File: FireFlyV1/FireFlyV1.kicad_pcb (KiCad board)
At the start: 2 copper layers, 64 x 26.2 mm, 59 parts, among them J1 Conn_01x03, J2 Conn_01x01_Pin, J3 Conn_01x01_Pin, SW1 TS-1187A-B-A-B, SW2 TS-1187A-B-A-B, U1 RP2040, U2 W25Q32JVSS, U3 AMS1117-3.3, U5 MCP6001T-I/OT, U7 PEC12R-4215F-S0024, X1 X322512MSB4SI

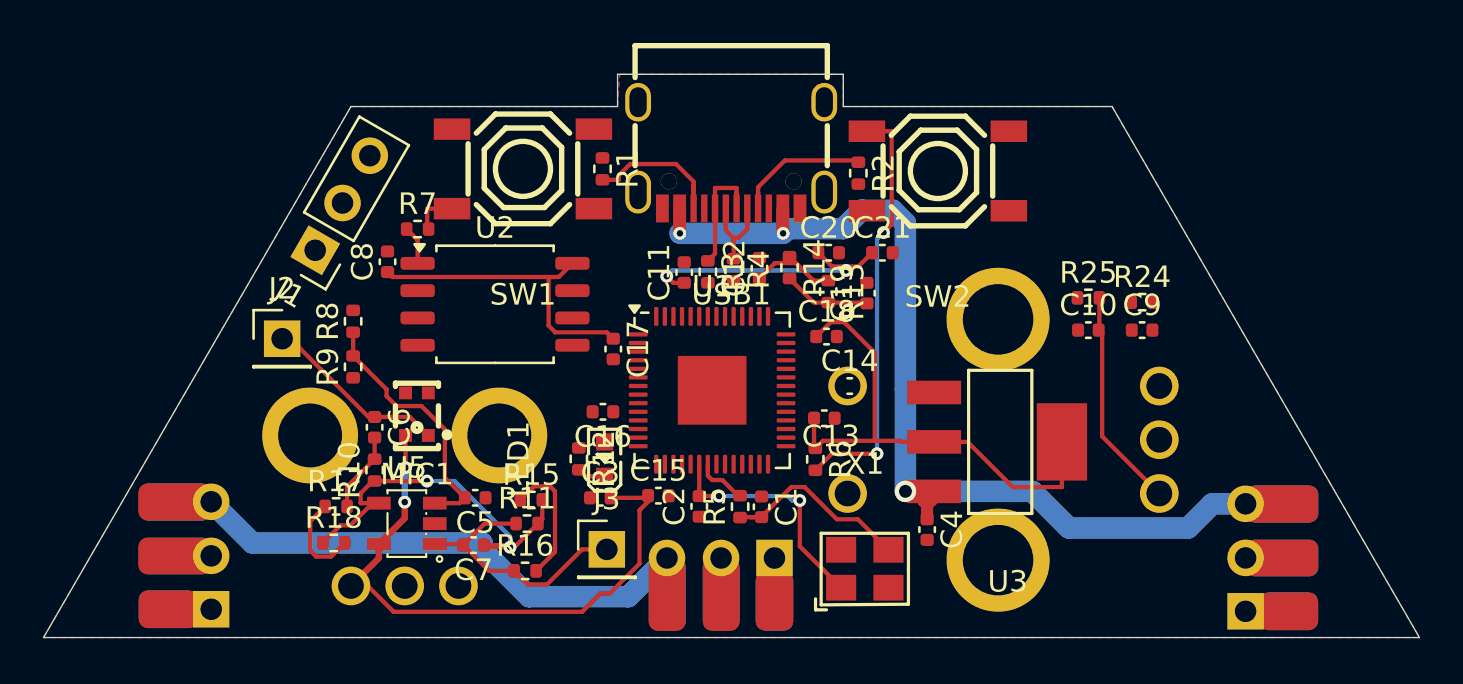
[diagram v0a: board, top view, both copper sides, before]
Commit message: Allowed the autorouter to try
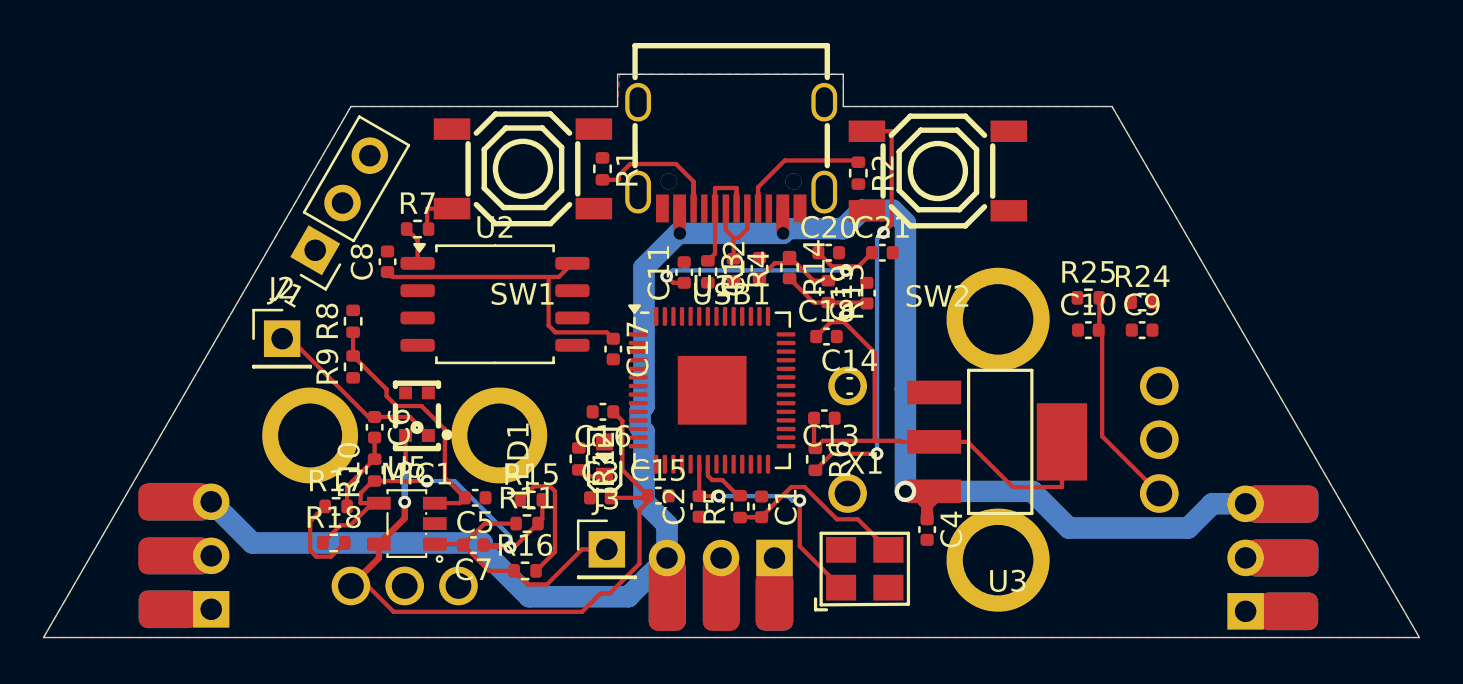
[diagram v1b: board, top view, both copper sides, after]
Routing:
- net +5V: track 78.6 -> 98.0 mm
- net 3V3: track 71.1 -> 75.9 mm

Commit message: First JLCPCB Order
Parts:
- moved C8 27.2 mm to (223.8, 113.0), turned to 180 degrees
- moved C21 17.5 mm to (209.1, 113.0), turned to 180 degrees
- moved R24 14.5 mm to (221.4, 110.5)
- moved C4 12.0 mm to (232.7, 105.8), turned to 90 degrees
- moved R25 11.7 mm to (221.5, 109.2)
- moved C3 11.3 mm to (208.3, 101.4), turned to 180 degrees
- moved MIC1 10.6 mm to (194.1, 117.4), turned to -90 degrees
- moved R9 9.67 mm to (203.1, 114.4), turned to 180 degrees
- moved C10 9.11 mm to (236.9, 112.3), turned to -90 degrees
- moved R8 7.99 mm to (200.6, 111.8), turned to 180 degrees
- moved X1 7.71 mm to (213.5, 116.3)
- moved C6 7.32 mm to (194.3, 115.5), turned to 180 degrees
- moved LEDS2 5.76 mm to (220.3, 118.9)
- moved R10 4.98 mm to (194.3, 114.3), turned to 180 degrees
- moved C9 4.16 mm to (237.0, 107.9), turned to -90 degrees
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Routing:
- net BOARD_ID_0: track 6.00 -> 51.5 mm, vias 0 -> 30
- net 3V3: track 75.9 -> 36.0 mm, vias 2 -> 15
- net SWCLK: track 0.00 -> 29.3 mm, vias 0 -> 1
- net POT_ADC: track 0.00 -> 28.4 mm, vias 0 -> 1
- net SWDIO: track 0.00 -> 25.2 mm, vias 0 -> 1
- net LED_OUT_3: track 3.40 -> 27.6 mm
- net LED_OUT_1: track 3.85 -> 24.6 mm, vias 0 -> 1
- net /A: track 0.00 -> 19.3 mm, vias 0 -> 1
- net BUTTON: track 0.00 -> 18.4 mm, vias 0 -> 2
- net QSPI_SS: track 1.81 -> 19.3 mm
- net QSPI_SD2: track 0.00 -> 15.5 mm, vias 0 -> 2
- net MIC_ADC: track 12.3 -> 27.7 mm, vias 0 -> 2
- net QSPI_SP1: track 0.00 -> 14.6 mm, vias 0 -> 2
- net +5V: track 98.0 -> 110.7 mm, vias 3 -> 2
- net Net-(U1-VREG_VOUT): track 12.6 -> 24.4 mm, vias 2 -> 5
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- added copper zone on In1.Cu, net 3V3
- added copper zone on B.Cu, net BOARD_ID_0
- added copper zone on In2.Cu, net BOARD_ID_0
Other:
- copper layers 2 -> 4
- board text added: "FireFlyV1 @KylarLEDs"
